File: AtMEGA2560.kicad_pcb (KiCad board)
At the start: 4 copper layers, 101.6 x 53.3 mm, 60 parts, among them IC1 NCP1117-5.0_SOT223, IC3 ATmega2560-16AU, IC4 ATmega16U2-AU, IC6 LP2985-3.3, IC7 LMV358IDGKR, T1 FDN340P, X1 DC21MMX, X2 USB-B_TH, Y1 CSTCE16M0V53-R0 16MHZ, Y2 16MHz

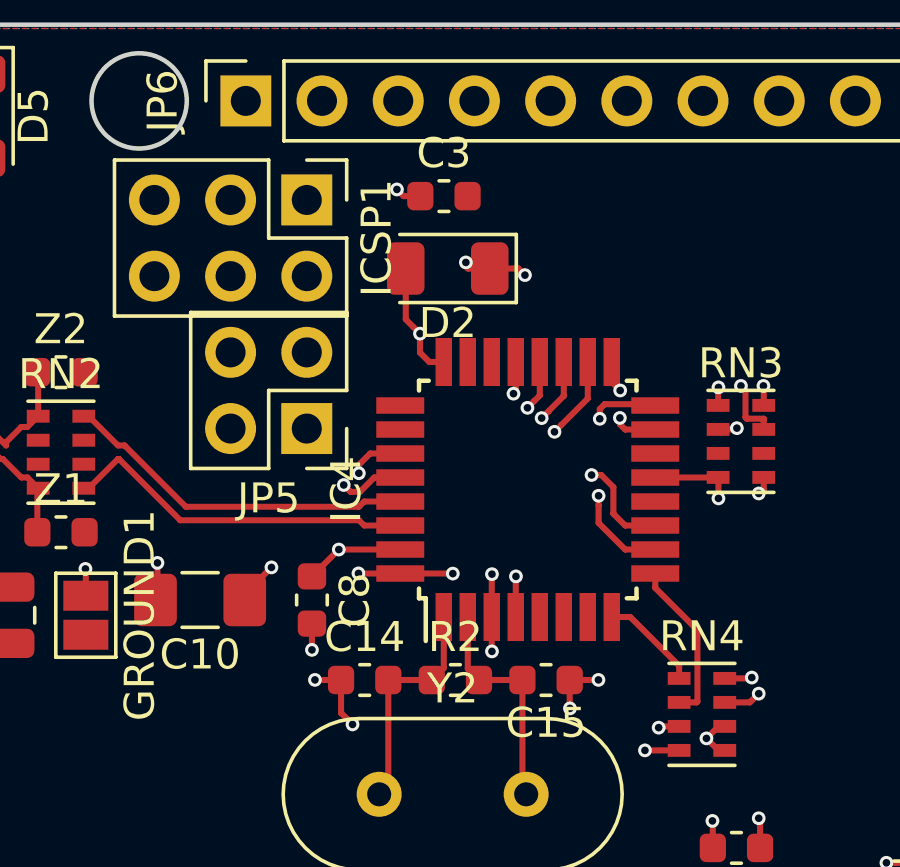
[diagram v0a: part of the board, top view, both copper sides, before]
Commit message: Cleaning up around the USB signals and added USB netname for shield and GND
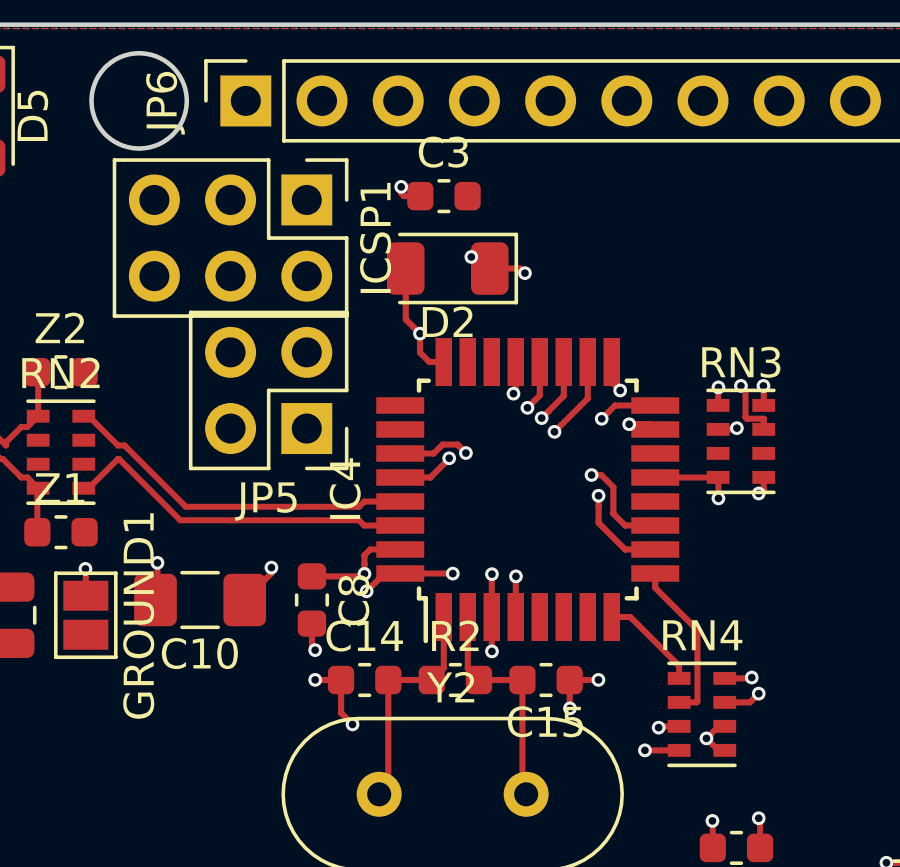
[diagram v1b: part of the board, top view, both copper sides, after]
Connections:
- net Net-(C10-Pad2) renamed /USBGND
- net Net-(F1-Pad2) renamed /VBUS
- net Net-(L1-Pad1) renamed /USBSHIELD
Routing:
- net ~RESET2~: track 57.8 -> 73.2 mm
- net Net-(C10-Pad1): track 7.89 -> 12.1 mm
- net /USBGND: track 26.3 -> 29.7 mm
- net /SCK2: track 17.4 -> 19.2 mm
- net USBVCC: track 26.6 -> 25.8 mm
- net /VBUS: track 29.3 -> 29.9 mm

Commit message: Initial USB floods
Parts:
- moved GROUND1 9.21 mm to (89.2, 79.1), turned to 90 degrees
- moved C10 2.47 mm to (91.5, 89.2), turned to 90 degrees
- moved L1 2.13 mm to (89.2, 87.4)
- moved Z2 1.91 mm to (87.2, 79.2), turned to 90 degrees
- moved Z1 1.88 mm to (87.2, 86.4), turned to 270 degrees
- moved RN2 1.13 mm to (87.7, 82.8)
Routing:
- net /VBUS: track 29.9 -> 1.09 mm
- net /USBGND: track 29.7 -> 3.86 mm, vias 4 -> 2
- net /USB2+: track 9.69 -> 7.39 mm
- net Net-(D5-Pad2): track 36.8 -> 34.9 mm
- net /USB2-: track 8.24 -> 6.39 mm
- net /USB1+: track 11.9 -> 13.4 mm
- net Net-(C10-Pad1): track 12.1 -> 10.7 mm, vias 2 -> 1
- net Net-(D6-Pad2): track 39.3 -> 38.1 mm
- added copper zone on In1.Cu, net /USBGND
- added copper zone on In1.Cu, net /USBSHIELD
- removed copper zone on In1.Cu, net GND

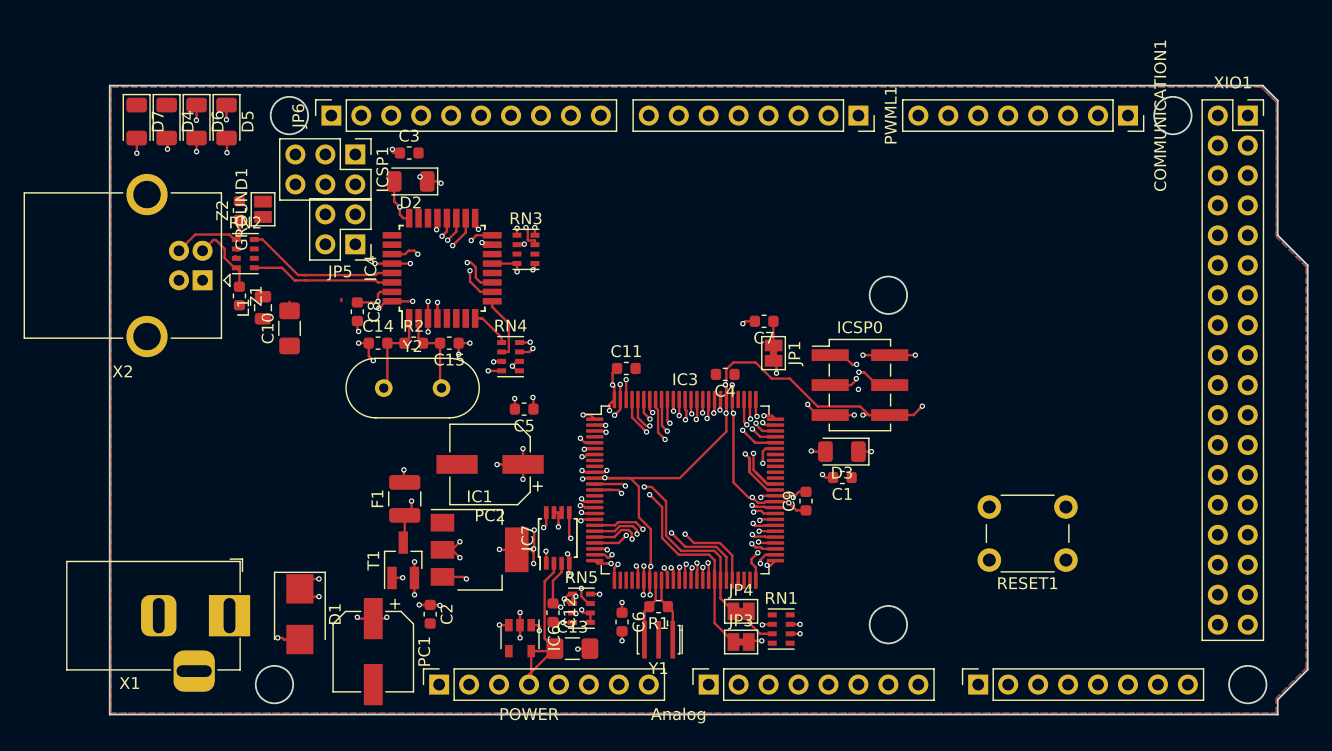
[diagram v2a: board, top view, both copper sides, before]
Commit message: Moved few parts for better 5VDC plane and moved some signals.
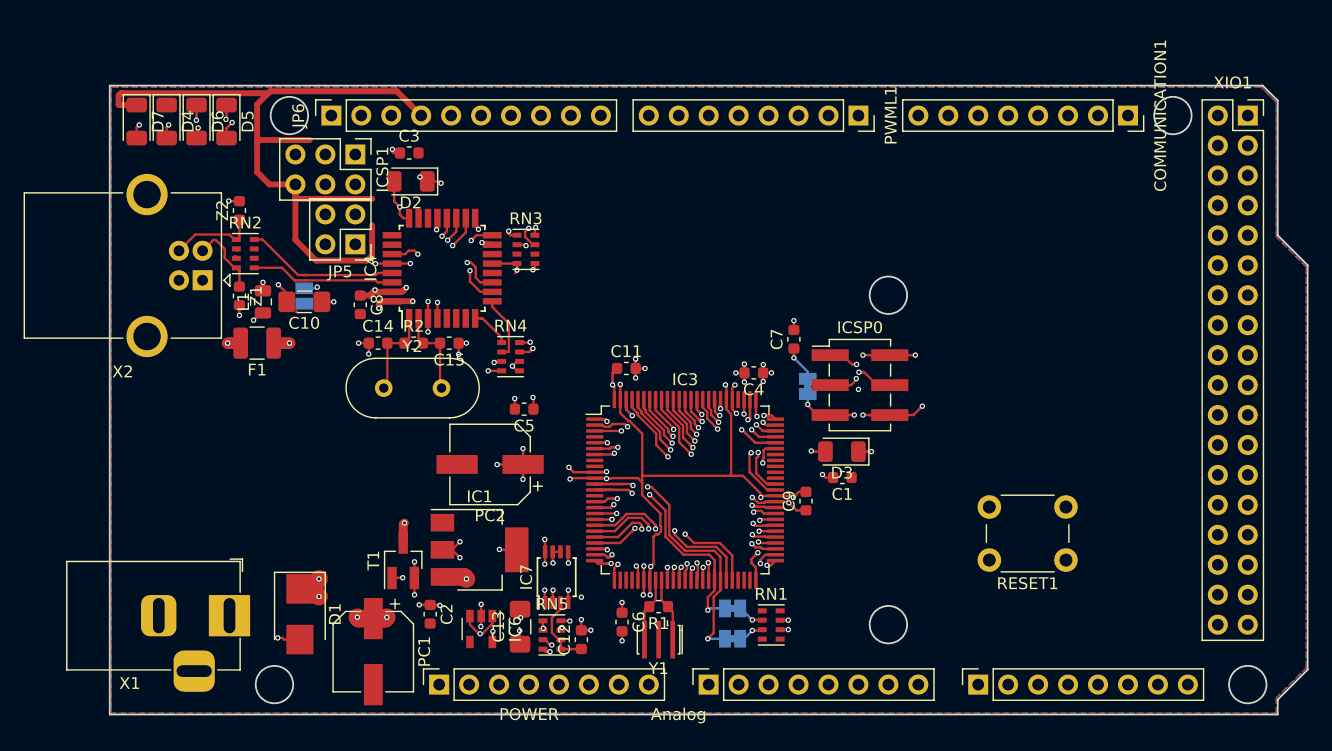
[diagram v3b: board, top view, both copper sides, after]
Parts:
- GROUND1, JP1, JP3, JP4: moved to B.Cu
- moved F1 18.2 mm to (88.7, 90.4), turned to 180 degrees
- moved GROUND1 8.14 mm to (92.7, 86.4), turned to 270 degrees
- moved C13 4.82 mm to (111.0, 114.5), turned to 90 degrees
- moved JP1 4.05 mm to (135.4, 94.1)
- moved IC6 3.39 mm to (107.7, 114.7)
- moved RN5 3.38 mm to (113.7, 115.2)
- moved IC7 3.33 mm to (114.1, 110.3)
- moved C12 3.32 mm to (116.2, 115.6), turned to 90 degrees
- moved C7 2.95 mm to (134.2, 90.1), turned to 90 degrees
- moved JP3 2.94 mm to (129.0, 112.9)
- moved C10 2.57 mm to (92.7, 86.9), turned to 180 degrees
- moved JP4 2.44 mm to (129.0, 115.5)
- moved C4 2.43 mm to (130.8, 92.9)
- moved RN1 0.92 mm to (132.3, 114.3)
- moved C8 0.64 mm to (97.5, 87.2)
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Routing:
- net GND: track 79.9 -> 145.4 mm, vias 28 -> 32
- net ~RESET~: track 79.6 -> 102.2 mm, vias 7 -> 6
- net +5V: track 68.5 -> 84.4 mm, vias 40 -> 38
- net +VDC: track 29.8 -> 44.0 mm
- net USBVCC: track 25.8 -> 35.9 mm, vias 2 -> 4
- net Net-(D5-Pad2): track 34.9 -> 43.9 mm
- net Net-(D6-Pad2): track 38.1 -> 46.8 mm
- net /VBUS: track 1.09 -> 7.31 mm
- net TXD0: track 56.3 -> 51.0 mm
- net TXD3: track 72.9 -> 67.7 mm
- net RXD3: track 72.4 -> 67.7 mm
- net /TXD1: track 70.4 -> 65.9 mm
- net ~HWB~: track 24.9 -> 29.3 mm
- net Net-(IC7-Pad6): track 27.7 -> 32.0 mm
- net /PE4: track 42.8 -> 38.7 mm
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- added copper zone on In2.Cu, net USBVCC
